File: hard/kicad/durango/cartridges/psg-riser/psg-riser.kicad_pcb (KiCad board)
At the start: 2 copper layers, 59.7 x 53.3 mm, 10 parts, among them J1 Durango_ROM, J2 CARTRIDGE, U1 SN76489A, U2 74HC574, U3 74HC138, U4 74HC08

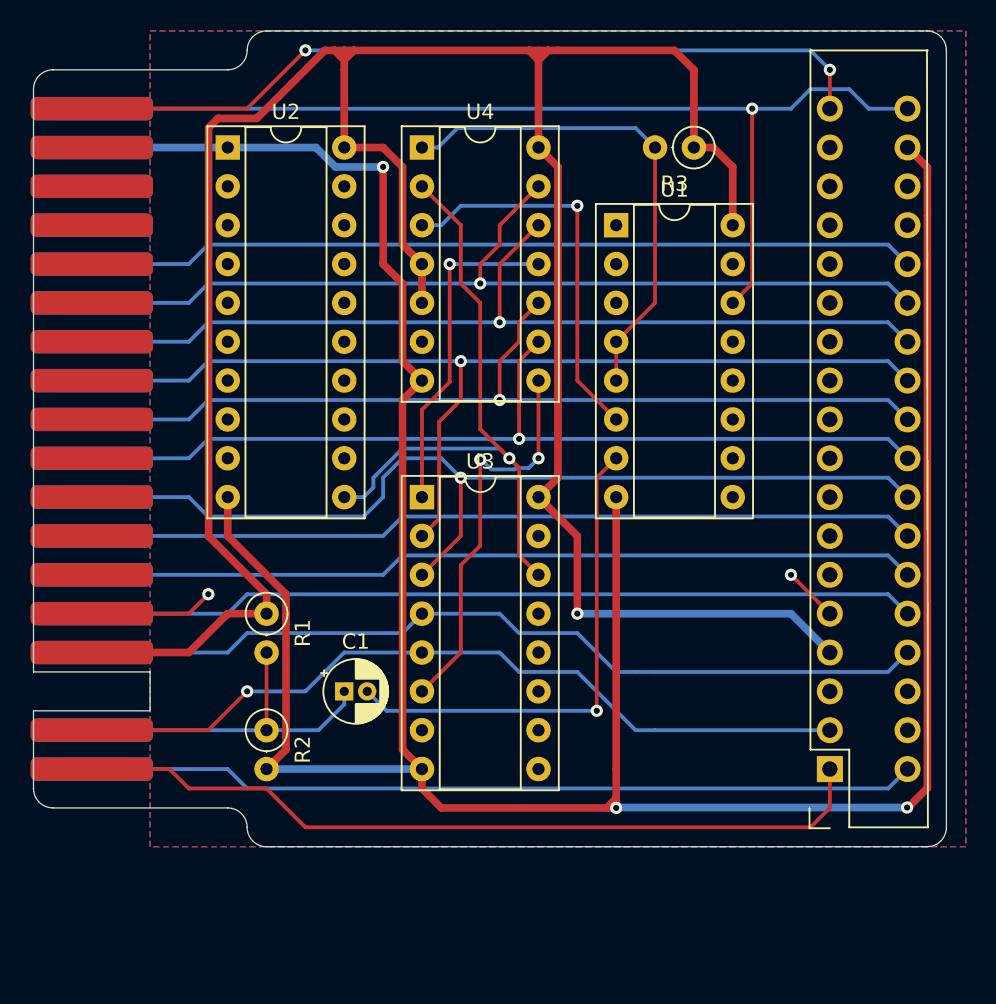
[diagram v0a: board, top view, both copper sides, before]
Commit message: rerouted PSG riser card
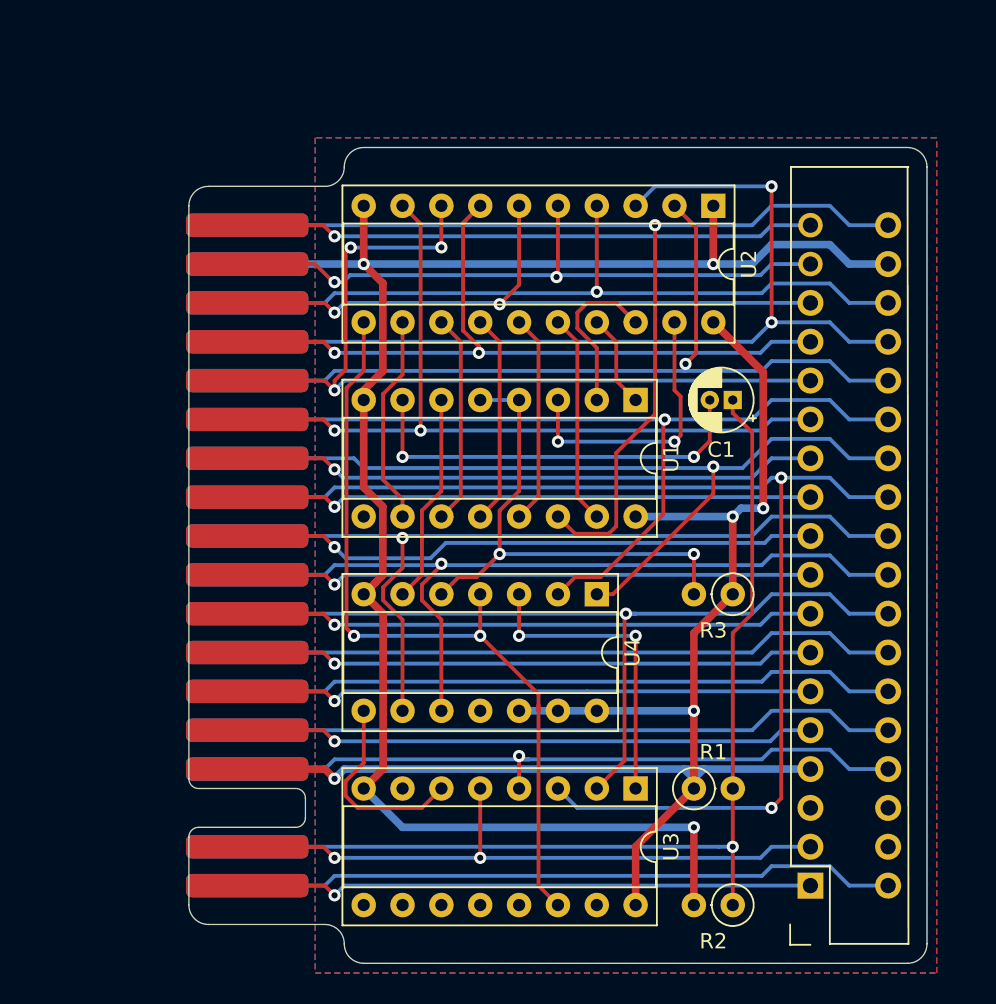
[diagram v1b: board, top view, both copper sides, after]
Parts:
- moved R2 32.6 mm to (61.0, 69.8), turned to 180 degrees
- moved U2 32.0 mm to (59.7, 24.1), turned to 270 degrees
- moved C1 31.8 mm to (61.0, 36.8), turned to 180 degrees
- moved U4 31.4 mm to (52.1, 49.5), turned to 270 degrees
- moved R1 30.2 mm to (58.4, 62.2), turned to 0 degrees
- moved R3 29.3 mm to (61.0, 49.5)
- moved U3 23.6 mm to (54.6, 62.2), turned to 270 degrees
- moved J1 12.7 mm to (25.4, 22.9)
- moved U1 11.5 mm to (54.6, 36.8), turned to 270 degrees
- moved J2 7.73 mm to (69.8, 71.8)
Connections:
- U3 pad 2: /A2 -> /A5
- U3 pad 3: /A5 -> /A2
- U4 pad 1: /RDY -> /A1
- U4 pad 10: /A3 -> /A4
- U4 pad 11: /A0·1 -> (no net)
- U4 pad 12: /A1 -> +5V
- U4 pad 13: /A0 -> +5V
- U4 pad 2: /~PSG -> /A0
- U4 pad 3: /~POE -> /A0·1
- U4 pad 4: +5V -> /~PSG
- U4 pad 5: +5V -> /RDY
- U4 pad 6: (no net) -> /~POE
- U4 pad 9: /A4 -> /A3
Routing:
- net GND: track 190.1 -> 115.7 mm
- net +5V: track 172.3 -> 102.0 mm, vias 1 -> 4
- net /D1: track 0.00 -> 61.3 mm, vias 0 -> 2
- net /D6: track 0.00 -> 55.8 mm, vias 0 -> 3
- net /D7: track 0.00 -> 52.6 mm, vias 0 -> 2
- net /D2: track 0.00 -> 48.6 mm, vias 0 -> 1
- net /D5: track 0.00 -> 47.9 mm, vias 0 -> 2
- net /D4: track 0.00 -> 44.3 mm, vias 0 -> 2
- net /AUDIO: track 23.1 -> 65.8 mm, vias 0 -> 1
- net /D3: track 0.00 -> 42.5 mm, vias 0 -> 2
- net /~OE: track 0.00 -> 38.0 mm, vias 0 -> 1
- net /~CS: track 0.00 -> 38.0 mm, vias 0 -> 1
- net /A9: track 0.00 -> 37.4 mm, vias 0 -> 1
- net /A8: track 0.00 -> 37.4 mm, vias 0 -> 1
- net /A11: track 0.00 -> 37.4 mm, vias 0 -> 1
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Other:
- board size 59.7 x 53.3 mm -> 48.3 x 53.3 mm

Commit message: revise PSG roser routing
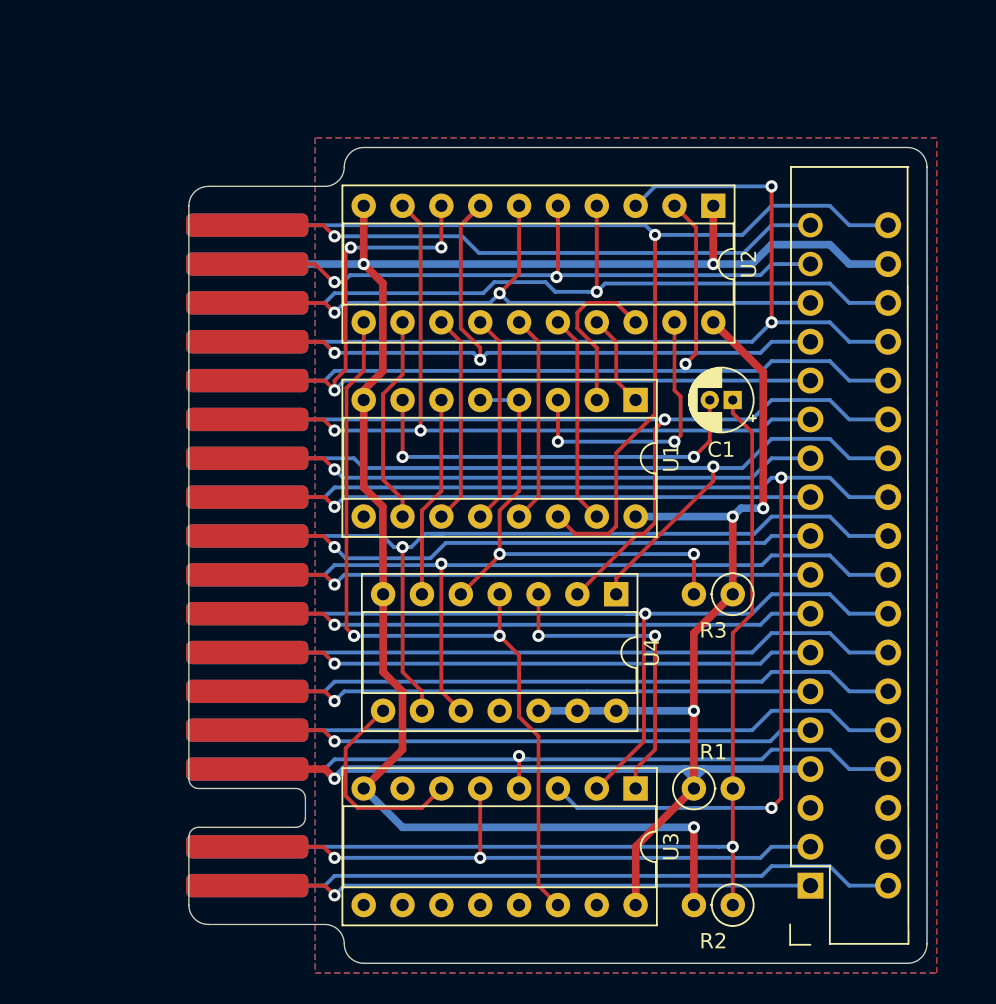
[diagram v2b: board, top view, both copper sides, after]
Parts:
- moved U4 1.27 mm to (53.3, 49.5)
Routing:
- net /D5: track 47.9 -> 50.5 mm
- net +5V: track 102.0 -> 100.7 mm
- net /RDY: track 33.4 -> 32.1 mm
- net /A0: track 58.3 -> 57.1 mm
- net /A1: track 55.6 -> 54.5 mm
- net /~RST: track 37.4 -> 38.3 mm
- net /A3: track 55.4 -> 56.3 mm
- net /D2: track 48.6 -> 49.1 mm
- net /A0·1: track 20.3 -> 20.8 mm
- net /~POE: track 13.8 -> 13.2 mm
- net /A3·4: track 13.2 -> 13.7 mm
- net /A5: track 55.8 -> 56.3 mm

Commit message: flip PSG data bits
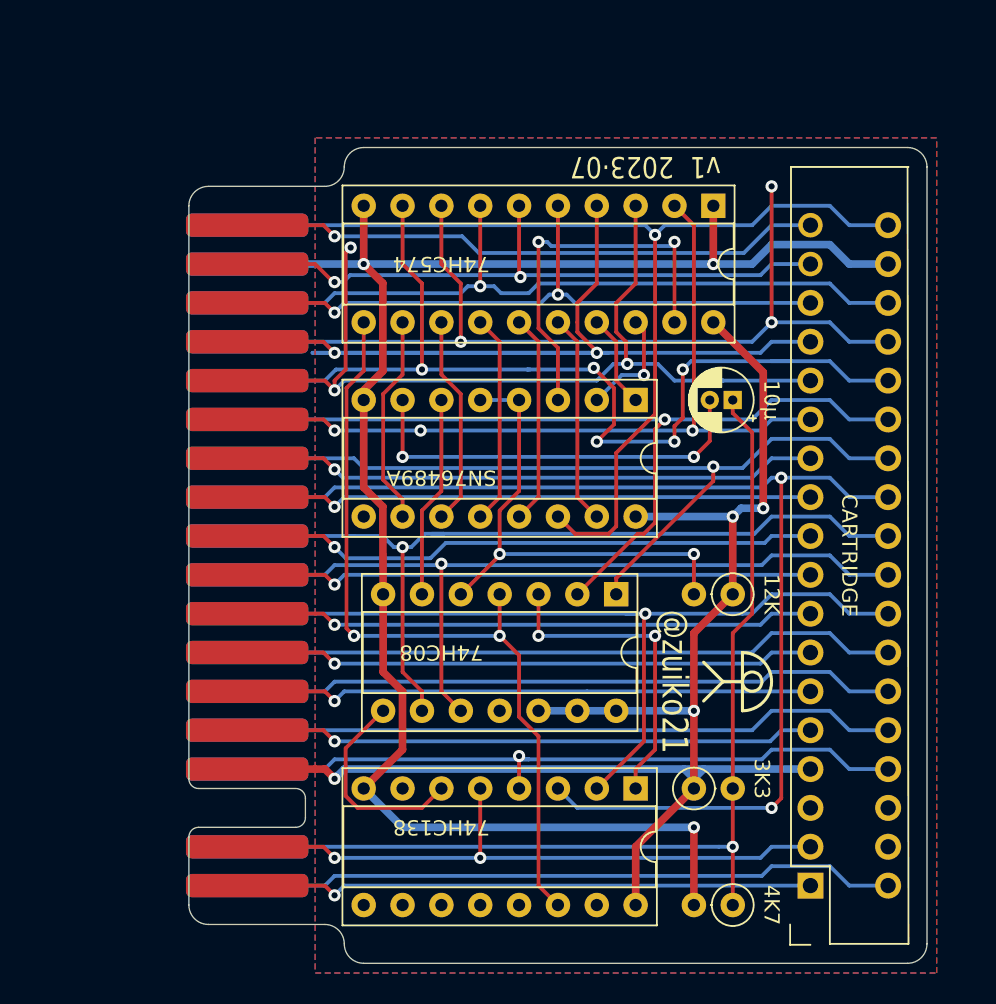
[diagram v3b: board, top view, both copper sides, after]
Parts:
- added LOGO1: Logo_Open_Hardware_Small, durango:j300, B.Cu at (60.7, 53.8)
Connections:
- net /LD0 renamed /B7
- net /LD1 renamed /B6
- net /LD2 renamed /B5
- net /LD3 renamed /B4
- net /LD4 renamed /B3
- net /LD5 renamed /B2
- net /LD6 renamed /B1
- net /LD7 renamed /B0
- U2 pad 2: /D0 -> /D7
- U2 pad 3: /D1 -> /D6
- U2 pad 4: /D2 -> /D5
- U2 pad 5: /D3 -> /D4
- U2 pad 6: /D4 -> /D3
- U2 pad 7: /D5 -> /D2
- U2 pad 8: /D6 -> /D1
- U2 pad 9: /D7 -> /D0
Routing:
- net /D5: track 50.5 -> 86.0 mm
- net /D0: track 54.7 -> 65.7 mm, vias 1 -> 5
- net /B7: track 18.5 -> 25.2 mm
- net /D6: track 55.8 -> 61.1 mm
- net /B6: track 10.8 -> 7.43 mm, vias 0 -> 1
- net /D2: track 49.1 -> 48.6 mm
- net /D7: track 52.6 -> 52.7 mm, vias 2 -> 3
- net /D1: vias 2 -> 3
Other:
- board text added: "@zuiko21"
- board text added: "SN76489A PSG riser card"
- board text added: "v1 2023·07"

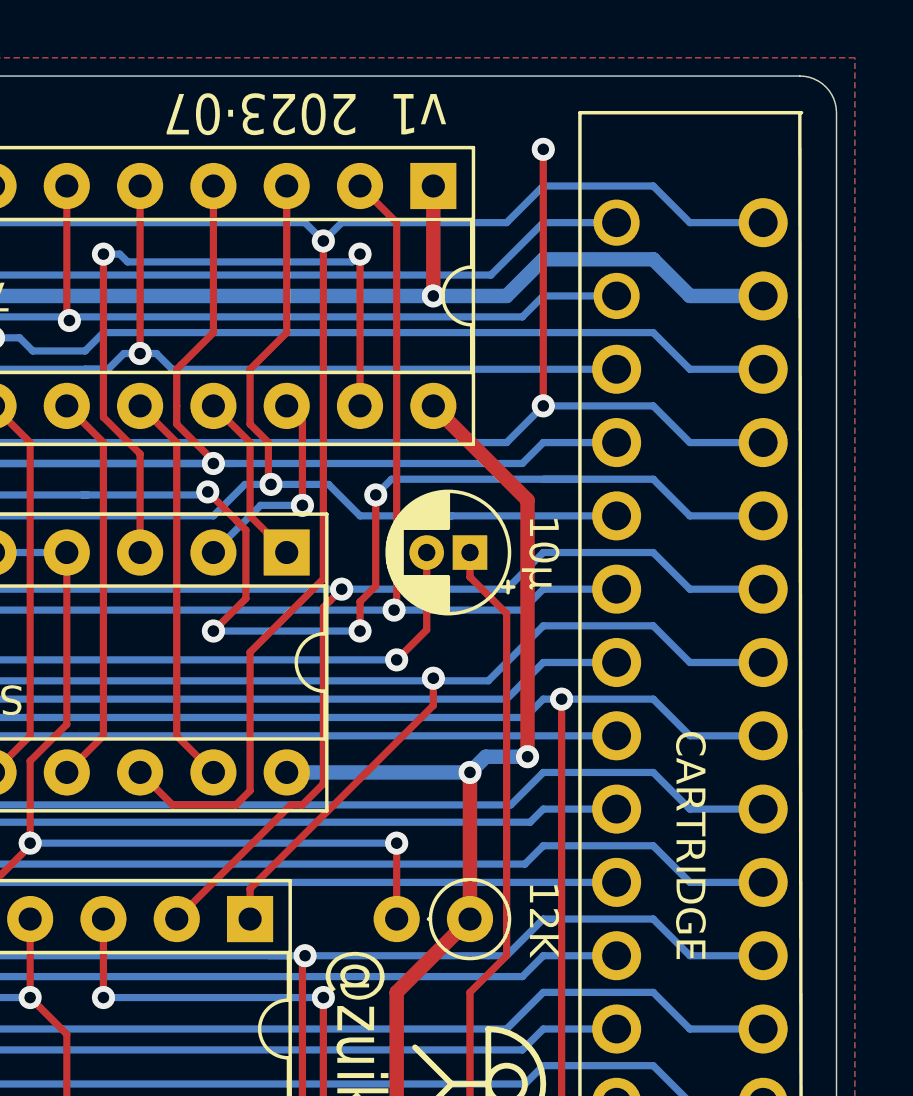
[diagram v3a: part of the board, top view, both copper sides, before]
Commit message: improve layout on PSG riser
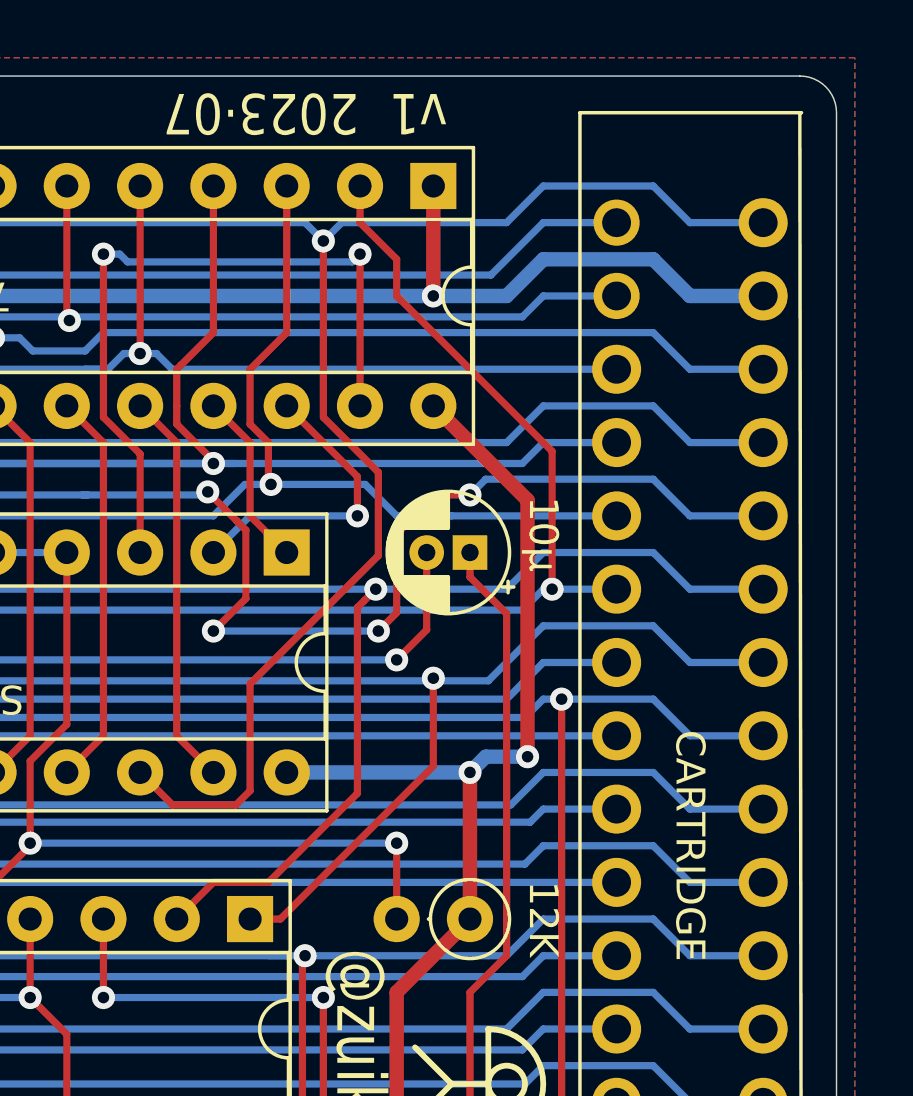
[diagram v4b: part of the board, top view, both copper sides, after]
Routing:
- net /D1: track 61.3 -> 52.4 mm, vias 3 -> 1
- net /B6: track 7.43 -> 10.3 mm
- net /D6: track 61.1 -> 59.2 mm
- net /D0: track 65.7 -> 63.9 mm
- net /VCLK: track 68.1 -> 69.6 mm
- net /D7: track 52.7 -> 54.2 mm
- net /A0: track 57.1 -> 58.4 mm
- net /A1: track 54.5 -> 55.1 mm

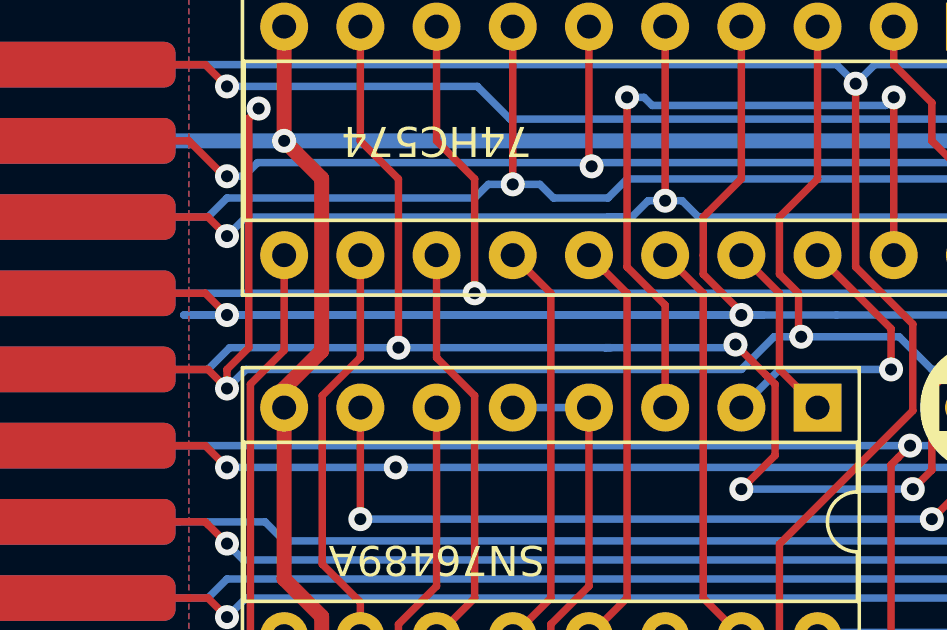
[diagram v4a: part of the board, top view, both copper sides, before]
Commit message: clean line in PSG PCB
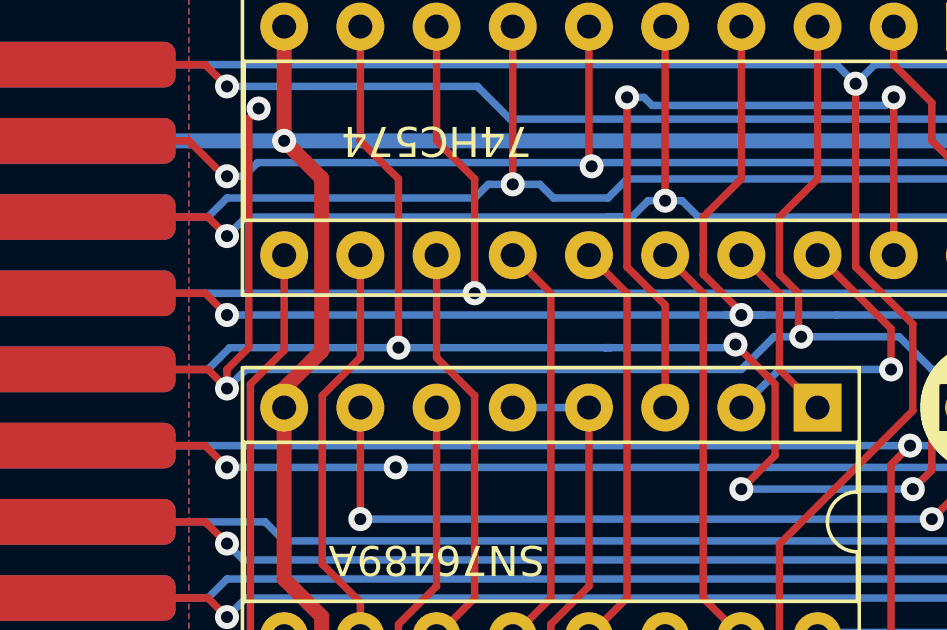
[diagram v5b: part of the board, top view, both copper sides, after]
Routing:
- net /D5: track 86.0 -> 49.4 mm
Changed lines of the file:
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@@
     (thickness 1.6)
     (drawings 31)
-    (tracks 505)
+    (tracks 503)
     (zones 0)
     (modules 11)
@@
   (segment (start 52.07 24.13) (end 52.07 29.21) (width 0.25) (layer F.Cu) (net 21))
   (segment (start 52.07 29.21) (end 50.944999 30.335001) (width 0.25) (layer F.Cu) (net 21))
-  (segment (start 34.925 33.745) (end 51.525 33.745) (width 0.25) (layer B.Cu) (net 21))
   (segment (start 50.944999 30.335001) (end 50.8 30.48) (width 0.25) (layer F.Cu) (net 21))
   (segment (start 50.8 30.48) (end 50.8 31.75) (width 0.25) (layer F.Cu) (net 21))
@@
   (segment (start 50.8 32.38359) (end 52.07 33.65359) (width 0.25) (layer F.Cu) (net 21))
   (segment (start 50.8 31.75) (end 50.8 32.38359) (width 0.25) (layer F.Cu) (net 21))
-  (segment (start 33.483452 33.745) (end 52.795 33.745) (width 0.25) (layer B.Cu) (net 21))
-  (segment (start 52.07 33.745) (end 33.483452 33.745) (width 0.25) (layer B.Cu) (net 21))
   (segment (start 52.795 33.745) (end 55.245 33.745) (width 0.25) (layer B.Cu) (net 21))
   (segment (start 51.525 33.745) (end 52.795 33.745) (width 0.25) (layer B.Cu) (net 21))
+  (segment (start 34.925 33.745) (end 52.795 33.745) (width 0.25) (layer B.Cu) (net 21))
   (via (at 34.925 36.195) (size 0.8) (drill 0.4) (layers F.Cu B.Cu) (net 22))
   (segment (start 34.29 35.56) (end 34.925 36.195) (width 0.25) (layer F.Cu) (net 22))

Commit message: revised PSG riser card
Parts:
- R3: value 12K -> 3K3
- moved R1 2.54 mm to (61.0, 62.2), turned to 180 degrees
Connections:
- R1 pad 1: +5V -> /AUDIO
- R1 pad 2: /AUDIO -> +5V
- U1 pad 5: /RDY -> GND
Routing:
- net GND: track 115.7 -> 126.1 mm, vias 3 -> 5
- net /RDY: track 32.1 -> 29.6 mm
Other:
- board text added: "AUDIO"
- board text added: "GND"
- board text added: "JLCJLCJLCJLC"
